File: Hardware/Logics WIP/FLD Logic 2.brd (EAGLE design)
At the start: 61 x 33.3 mm, 88 parts

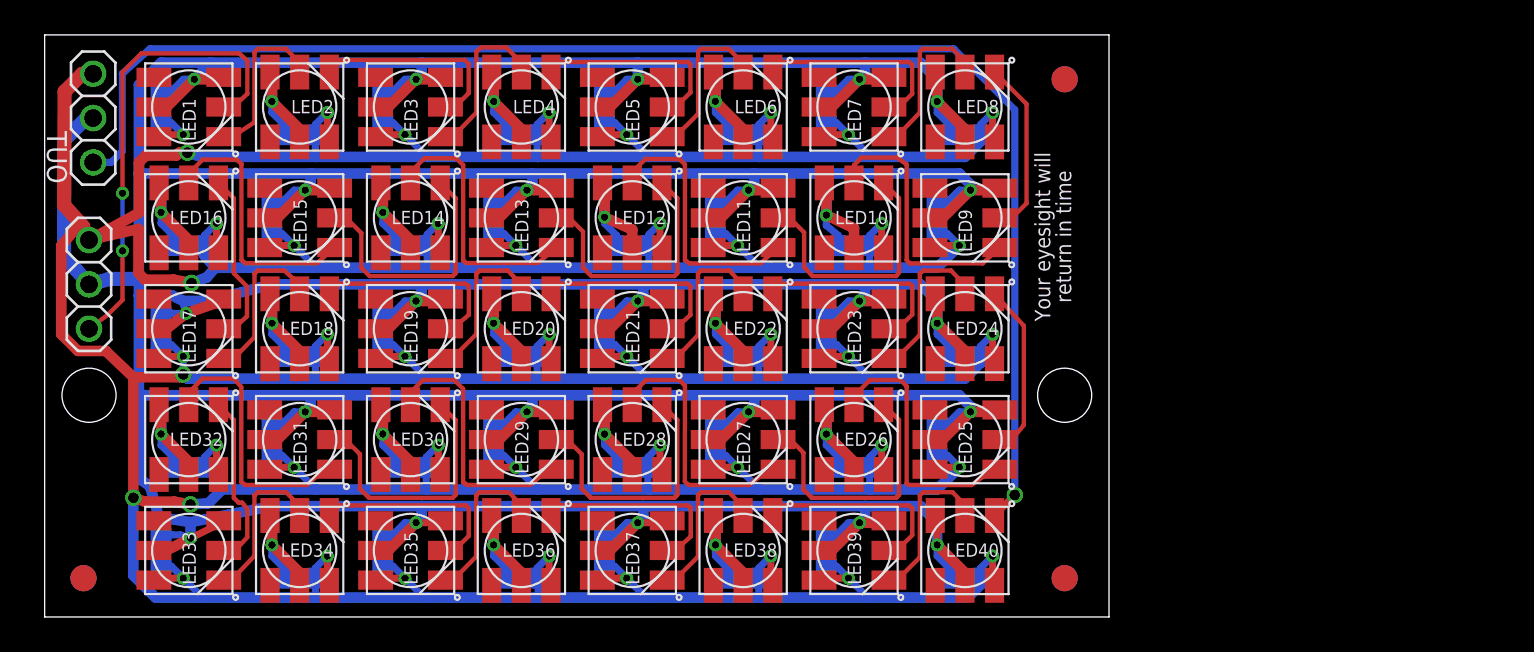
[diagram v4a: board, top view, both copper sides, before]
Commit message: 
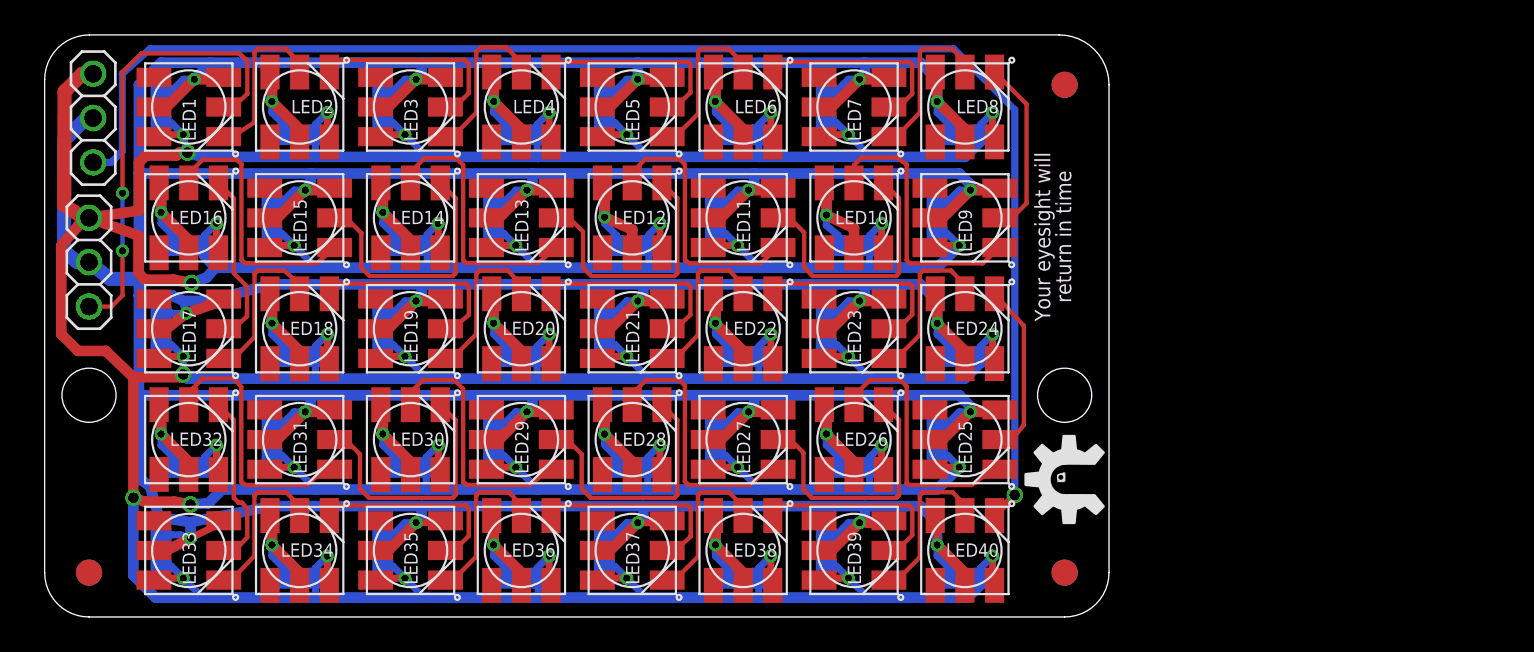
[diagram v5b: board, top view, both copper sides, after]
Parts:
- removed FID1, FID2, FID3, FID4, FID5, FID6: FIDUCIAL1.5X3, SparkFun-Aesthetics:FIDUCIAL-1.5X3
- added FID10, FID11, FID12, FID7, FID8, FID9: (no value), SmallBatchLibPre1:FIDUCIAL_G15
- added U$1: (no value), rseries:ROYAL-ENGINEERS-OF-NABOO-BOTTOM-LARGE
- added U$2, U$3: (no value), rseries:RSERIES-OSHW-LOGO-MEDIUM-BOTTOM
- moved IN 1.27 mm to (2.54, 20.3)
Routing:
- net DIN: track 26.9 -> 26.3 mm
- net +5V: track 609.0 -> 608.5 mm
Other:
- outline, holes or cut-outs redrawn
- board text added: "2013-10-10"
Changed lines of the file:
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@@
 <setting verticaltext="up"/>
 </settings>
-<grid distance="0.00125" unitdist="inch" unit="inch" style="lines" multiple="1" display="yes" altdistance="0.0625" altunitdist="inch" altunit="inch"/>
+<grid distance="0.01" unitdist="inch" unit="inch" style="lines" multiple="1" display="yes" altdistance="0.0625" altunitdist="inch" altunit="inch"/>
 <layers>
 <layer number="1" name="Top" color="4" fill="1" visible="yes" active="yes"/>
@@
 <board>
 <plain>
-<text x="1.5875" y="31.4325" size="1.397" layer="26" font="vector" rot="MR270">+ -</text>
-<text x="1.595" y="23.15375" size="1.397" layer="26" font="vector" rot="MR270">+ -</text>
-<wire x1="0" y1="0" x2="0" y2="33.3375" width="0" layer="20"/>
-<wire x1="0" y1="33.3375" x2="60.96" y2="33.3375" width="0" layer="20"/>
-<wire x1="60.96" y1="33.3375" x2="60.96" y2="0" width="0" layer="20"/>
-<wire x1="60.96" y1="0" x2="0" y2="0" width="0" layer="20"/>
+<text x="1.5875" y="31.9405" size="1.397" layer="26" font="vector" ratio="12" rot="MR270">+ -</text>
+<text x="1.341" y="23.66175" size="1.397" layer="26" font="vector" ratio="12" rot="MR270">+ -</text>
+<wire x1="0" y1="2.54" x2="0" y2="30.777734375" width="0" layer="20"/>
+<wire x1="0" y1="30.777734375" x2="2.559765625" y2="33.3375" width="0" layer="20" curve="-90"/>
+<wire x1="2.559765625" y1="33.3375" x2="58.1025" y2="33.3375" width="0" layer="20"/>
+<wire x1="58.1025" y1="33.3375" x2="60.96" y2="30.48" width="0" layer="20" curve="-90"/>
+<wire x1="60.96" y1="30.48" x2="60.96" y2="2.54" width="0" layer="20"/>
+<wire x1="60.96" y1="2.54" x2="58.42" y2="0" width="0" layer="20" curve="-90"/>
+<wire x1="58.42" y1="0" x2="2.54" y2="0" width="0" layer="20"/>
+<wire x1="2.54" y1="0" x2="0" y2="2.54" width="0" layer="20" curve="-90"/>
 <hole x="2.54" y="12.7" drill="3.1"/>
 <hole x="58.42" y="12.7" drill="3.1"/>
 <text x="57.75325" y="21.7805" size="0.889" layer="21" font="vector" distance="35" rot="R90" align="center">Your eyesight will
 return in time</text>
+<text x="58.42" y="27.559" size="1.27" layer="22" font="vector" ratio="12" rot="SMR270">2013-10-10</text>
 </plain>
 <attributes>
@@
 <element name="LED40" library="rseries" package="WS2812" value="WS2812" x="52.705" y="3.81" rot="R90"/>
 <element name="C40" library="SparkFun-Capacitors" package="0805" value="0.1uF" x="52.705" y="2.2225" smashed="yes" rot="MR180"/>
-<element name="FID1" library="SparkFun-Aesthetics" package="FIDUCIAL-1.5X3" value="FIDUCIAL1.5X3" x="58.42" y="30.7975"/>
-<element name="FID2" library="SparkFun-Aesthetics" package="FIDUCIAL-1.5X3" value="FIDUCIAL1.5X3" x="2.2225" y="2.2225"/>
-<element name="FID3" library="SparkFun-Aesthetics" package="FIDUCIAL-1.5X3" value="FIDUCIAL1.5X3" x="58.42" y="2.2225"/>
-<element name="FID4" library="SparkFun-Aesthetics" package="FIDUCIAL-1.5X3" value="FIDUCIAL1.5X3" x="58.42" y="30.7975" rot="MR0"/>
-<element name="FID5" library="SparkFun-Aesthetics" package="FIDUCIAL-1.5X3" value="FIDUCIAL1.5X3" x="58.42" y="2.2225" rot="MR0"/>
-<element name="FID6" library="SparkFun-Aesthetics" package="FIDUCIAL-1.5X3" value="FIDUCIAL1.5X3" x="2.2225" y="2.2225" rot="MR0"/>
-<element name="IN" library="adafruit" package="1X03" value="" x="2.54" y="19.05" smashed="yes" rot="R270">
-<attribute name="NAME" x="0.97155" y="17.4117" size="1.143" layer="26" font="vector" ratio="10" rot="MR270"/>
-<attribute name="VALUE" x="-0.635" y="22.86" size="1.27" layer="27" rot="R270"/>
+<element name="IN" library="adafruit" package="1X03" value="" x="2.54" y="20.32" smashed="yes" rot="R270">
+<attribute name="NAME" x="1.143" y="18.669" size="1.016" layer="26" font="vector" ratio="12" rot="MR270"/>
+<attribute name="VALUE" x="-0.635" y="24.13" size="1.27" layer="27" rot="R270"/>
 </element>
 <element name="OUT" library="adafruit" package="1X03" value="" x="2.778125" y="28.575" smashed="yes" rot="R270">
-<attribute name="NAME" x="1.273175" y="27.8257" size="1.143" layer="25" font="vector" ratio="10" rot="MR270"/>
+<attribute name="NAME" x="1.27" y="27.559" size="1.016" layer="26" font="vector" ratio="12" rot="MR270"/>
 <attribute name="VALUE" x="-0.396875" y="32.385" size="1.27" layer="27" rot="R270"/>
 </element>
+<element name="FID7" library="SmallBatchLibPre1" package="FIDUCIAL_G15" value="" x="2.54" y="2.54"/>
+<element name="FID8" library="SmallBatchLibPre1" package="FIDUCIAL_G15" value="" x="58.42" y="30.48"/>
+<element name="FID9" library="SmallBatchLibPre1" package="FIDUCIAL_G15" value="" x="58.42" y="2.54"/>
+<element name="FID10" library="SmallBatchLibPre1" package="FIDUCIAL_G15" value="" x="2.54" y="2.54" rot="MR0"/>
+<element name="FID11" library="SmallBatchLibPre1" package="FIDUCIAL_G15" value="" x="58.42" y="2.54" rot="MR0"/>
+<element name="FID12" library="SmallBatchLibPre1" package="FIDUCIAL_G15" value="" x="58.42" y="30.48" rot="MR0"/>
+<element name="U$1" library="rseries" package="ROYAL-ENGINEERS-OF-NABOO-BOTTOM-LARGE" value="" x="30.48" y="0"/>
+<element name="U$2" library="rseries" package="RSERIES-OSHW-LOGO-MEDIUM-BOTTOM" value="" x="59.69" y="7.874" rot="R90"/>
+<element name="U$3" library="rseries" package="RSERIES-OSHW-LOGO-MEDIUM-BOTTOM" value="" x="1.27" y="7.62" rot="MR90"/>
 </elements>
 <signals>
@@
 <contactref element="IN" pad="1"/>
 <contactref element="OUT" pad="1"/>
-<wire x1="2.19075" y1="22.38375" x2="1.905" y2="22.38375" width="0.6096" layer="1"/>
+<wire x1="2.19075" y1="22.89175" x2="1.905" y2="22.38375" width="0.6096" layer="1"/>
 <wire x1="2.778125" y1="31.115" x2="2.159" y2="31.115" width="0.8128" layer="1"/>
 <wire x1="2.159" y1="31.115" x2="1.143" y2="30.099" width="0.8128" layer="1"/>
 <wire x1="1.143" y1="30.099" x2="1.11125" y2="23.59025" width="0.8128" layer="1"/>
-<wire x1="1.11125" y1="23.59025" x2="2.19075" y2="22.38375" width="0.8128" layer="1"/>
-<wire x1="2.19075" y1="22.38375" x2="2.54" y2="21.59" width="0.8128" layer="1"/>
+<wire x1="1.11125" y1="23.59025" x2="2.19075" y2="22.89175" width="0.8128" layer="1"/>
+<wire x1="2.19075" y1="22.89175" x2="2.54" y2="22.86" width="0.8128" layer="1"/>
 <wire x1="5.08" y1="13.731875" x2="7.77875" y2="13.731875" width="0.6096" layer="1"/>
 <wire x1="7.77875" y1="13.731875" x2="7.9375" y2="13.890625" width="0.6096" layer="1"/>
@@
 <wire x1="7.540625" y1="26.431875" x2="5.794375" y2="26.431875" width="0.6096" layer="1"/>
 <wire x1="5.794375" y1="26.431875" x2="5.3975" y2="26.035" width="0.6096" layer="1"/>
-<wire x1="5.3975" y1="26.035" x2="5.3975" y2="23.14575" width="0.6096" layer="1"/>
-<wire x1="5.3975" y1="23.14575" x2="2.54" y2="21.59" width="0.6096" layer="1"/>
+<wire x1="5.3975" y1="26.035" x2="5.3975" y2="23.27275" width="0.6096" layer="1"/>
+<wire x1="5.3975" y1="23.27275" x2="2.54" y2="22.86" width="0.6096" layer="1"/>
 <wire x1="9.763125" y1="20.0025" x2="9.286875" y2="19.446875" width="0.6096" layer="16"/>
 <wire x1="9.286875" y1="19.446875" x2="8.41375" y2="19.129375" width="0.6096" layer="16"/>
@@
 <wire x1="7.381875" y1="19.319875" x2="5.72135" y2="19.319875" width="0.6096" layer="1"/>
 <wire x1="5.72135" y1="19.319875" x2="5.3721" y2="19.7231" width="0.6096" layer="1"/>
-<wire x1="5.3721" y1="19.7231" x2="5.3721" y2="22.225" width="0.6096" layer="1"/>
-<wire x1="5.3721" y1="22.225" x2="2.54" y2="21.59" width="0.6096" layer="1"/>
+<wire x1="5.3721" y1="19.7231" x2="5.3721" y2="21.844" width="0.6096" layer="1"/>
+<wire x1="5.3721" y1="21.844" x2="2.54" y2="22.86" width="0.6096" layer="1"/>
 <wire x1="9.763125" y1="20.0025" x2="9.155" y2="20.69" width="0.6096" layer="16"/>
 <wire x1="9.155" y1="20.69" x2="9.155" y2="21.2725" width="0.6096" layer="16"/>
@@
 <wire x1="10.16" y1="7.3025" x2="10.16" y2="7.5675" width="0.4064" layer="16"/>
 <wire x1="10.16" y1="7.5675" x2="9.155" y2="8.5725" width="0.4064" layer="16"/>
-<wire x1="8.175625" y1="26.590625" x2="7.9375" y2="27.6225" width="0" layer="19" extent="16-16"/>
+<wire x1="8.175625" y1="26.590625" x2="7.9375" y2="27.6225" width="0.4064" layer="16"/>
 </signal>
 <signal name="+5V" class="1">
@@
 <wire x1="2.778125" y1="28.575" x2="2.38125" y2="28.575" width="0.8128" layer="16"/>
 <wire x1="2.38125" y1="28.575" x2="1.11125" y2="27.305" width="0.8128" layer="16"/>
-<wire x1="1.11125" y1="27.305" x2="1.11125" y2="20.574" width="0.8128" layer="16"/>
-<wire x1="1.11125" y1="20.574" x2="1.8415" y2="19.84375" width="0.8128" layer="16"/>
-<wire x1="1.8415" y1="19.84375" x2="2.54" y2="19.05" width="0.8128" layer="16"/>
+<wire x1="1.11125" y1="27.305" x2="1.11125" y2="20.955" width="0.8128" layer="16"/>
+<wire x1="1.11125" y1="20.955" x2="1.8415" y2="20.35175" width="0.8128" layer="16"/>
+<wire x1="1.8415" y1="20.35175" x2="2.54" y2="20.32" width="0.8128" layer="16"/>
 <wire x1="44.655" y1="24.86" x2="44.7675" y2="24.7475" width="0.6096" layer="1"/>
 <wire x1="44.7675" y1="24.7475" x2="44.7675" y2="23.01875" width="0.6096" layer="1"/>
@@
 <wire x1="52.705" y1="15.24" x2="51.1175" y2="16.8275" width="0.6096" layer="1"/>
 <wire x1="5.3975" y1="19.3675" x2="3.7465" y2="19.3675" width="0.8128" layer="16"/>
-<wire x1="3.7465" y1="19.3675" x2="2.54" y2="19.05" width="0.8128" layer="16"/>
+<wire x1="3.7465" y1="19.3675" x2="2.54" y2="20.32" width="0.8128" layer="16"/>
 <wire x1="5.3975" y1="18.415" x2="5.3975" y2="19.3675" width="0.6096" layer="16"/>
 <wire x1="10.556875" y1="18.415" x2="8.89" y2="18.0975" width="0.6096" layer="16"/>
@@
 <wire x1="4.4577" y1="24.2697" x2="4.4577" y2="20.9677" width="0.254" layer="16"/>
 <via x="4.4577" y="20.9677" extent="1-16" drill="0.4064"/>
-<wire x1="4.4577" y1="20.9677" x2="4.4577" y2="18.15465" width="0.254" layer="1"/>
-<wire x1="4.4577" y1="18.15465" x2="3.6068" y2="17.30375" width="0.254" layer="1"/>
-<wire x1="3.6068" y1="17.30375" x2="2.54" y2="16.51" width="0.254" layer="1"/>
+<wire x1="4.4577" y1="20.9677" x2="4.4577" y2="18.40865" width="0.254" layer="1"/>
+<wire x1="4.4577" y1="18.40865" x2="3.82905" y2="17.78" width="0.254" layer="1"/>
+<wire x1="3.82905" y1="17.78" x2="2.54" y2="17.78" width="0.254" layer="1"/>
 </signal>
 <signal name="N$1">
